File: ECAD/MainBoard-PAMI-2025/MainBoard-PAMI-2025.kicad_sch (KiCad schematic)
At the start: 53 parts, among them J1 Sensor_Center, J10 Serial, J11 Con_Batt, J13 OLED, J2 USB_B, J3 Sensor_RIGHT, J4 Servo, J5 Sensor_LEFT, J6 Servo, J7 LeftMotor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

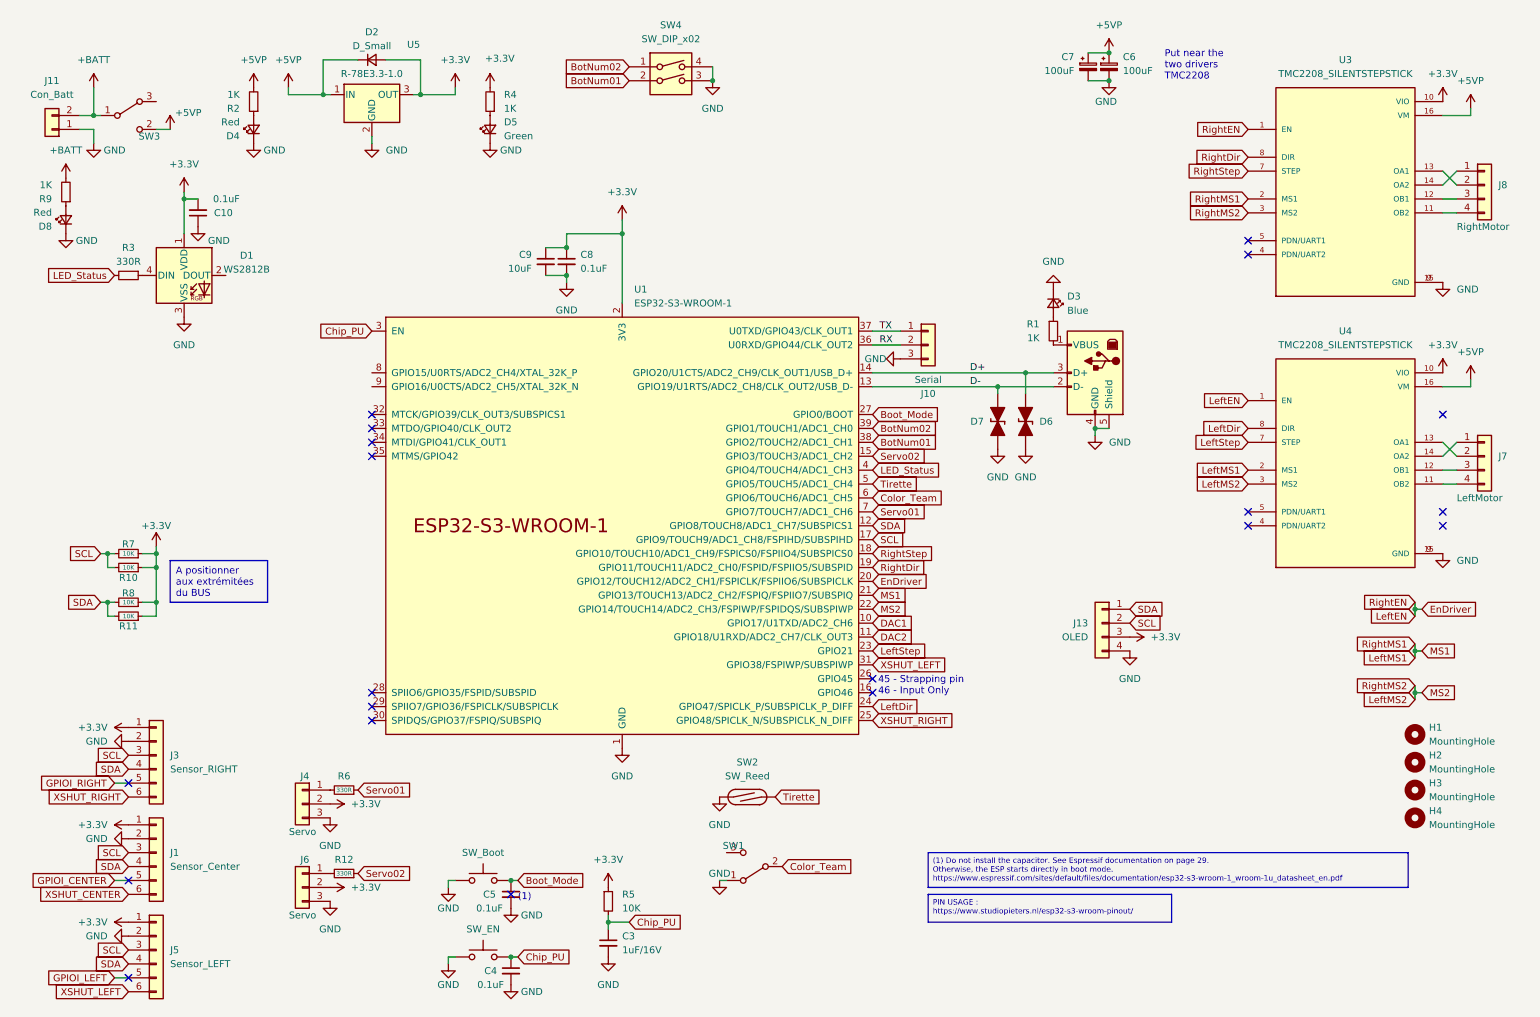
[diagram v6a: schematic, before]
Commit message: Update Live 206
Update Battery
Add Recom 5V
Add ASM1117
Add capacitor
Change sensor header
Move components
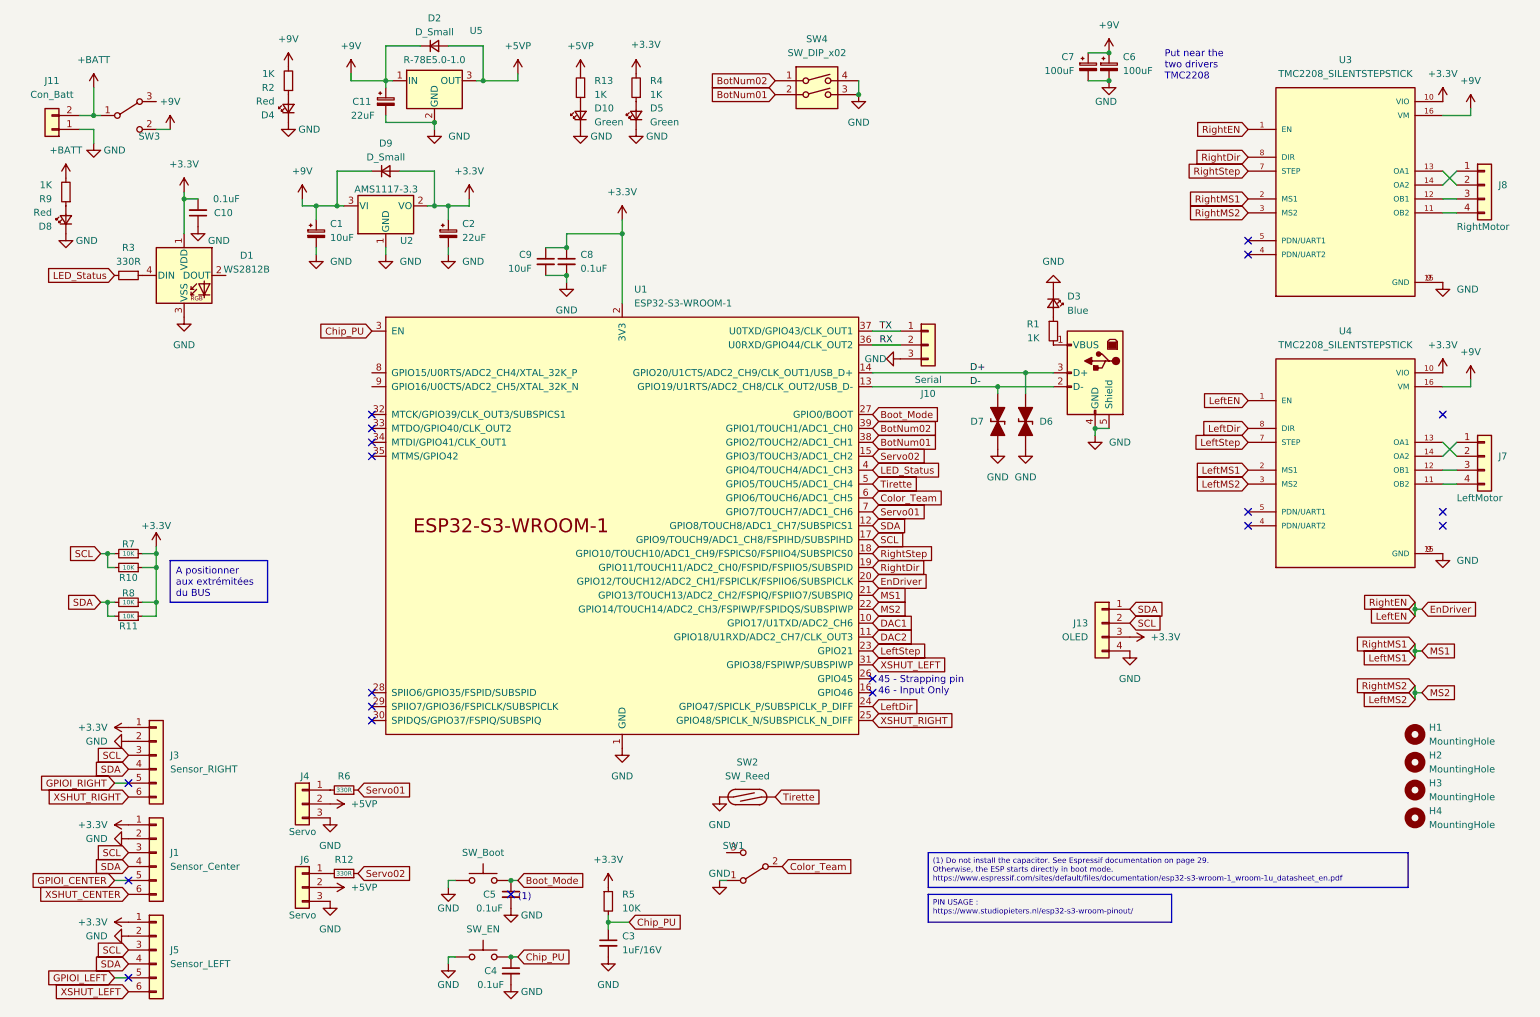
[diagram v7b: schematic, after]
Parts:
- added C1: 10uF, Capacitor_SMD:CP_Elec_5x5.4, symbol Device:C_Polarized_Small
- added C11: 22uF, Capacitor_SMD:CP_Elec_5x5.4, symbol Device:CP_Small
- added C2: 22uF, Capacitor_Tantalum_SMD:CP_EIA-3528-12_Kemet-T_Pad1.50x2.35mm_HandSolder, symbol Device:C_Polarized_Small
- added D10: Green, LED_SMD:LED_1206_3216Metric, symbol Device:LED_Small
- added D9: D_Small, Diode_SMD:D_SMA_Handsoldering, symbol Device:D_Small
- added R13: 1K, Resistor_SMD:R_1206_3216Metric_Pad1.30x1.75mm_HandSolder, symbol Device:R_Small
- added U2: AMS1117-3.3, Package_TO_SOT_SMD:SOT-223-3_TabPin2, symbol Regulator_Linear:AMS1117-3.3
- J1, J3, J5: footprint Connector_PinSocket_2.54mm:PinSocket_1x06_P2.54mm_Vertical -> PAMI-2025:VL53 Bottom Entry Version
- J11: footprint PAMI-2025:LP-e6 Batterie -> Connector_Molex:Molex_KK-254_AE-6410-02A_1x02_P2.54mm_Vertical
- U5: value R-78E3.3-1.0 -> R-78E5.0-1.0
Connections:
- net +3.3V: now also C2.1, D9.2 (A), U2.2 (VO); no longer D2.2 (A), J4.2 (Pin_2), J6.2 (Pin_2), U5.3 (OUT)
- net +5VP: now also D2.2 (A), J4.2 (Pin_2), J6.2 (Pin_2), U5.3 (OUT), R13.2; no longer C6.1, C7.1, D2.1 (K), R2.2, SW3.2 (C), U3.16 (VM), U4.16 (VM), U5.1 (IN)
- net GND: now also C1.2, C11.2, C2.2, D10.1 (K), U2.1 (GND)
- new net: D10.2 (A), R13.1
- new net +9V: C1.1, C11.1, C6.1, C7.1, D2.1 (K), D9.1 (K), R2.2, SW3.2 (C), U2.3 (VI), U3.16 (VM), U4.16 (VM), U5.1 (IN)
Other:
- moved on the sheet: D2, D4, D5, R2, R4, SW4, U5

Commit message: Add buzzer
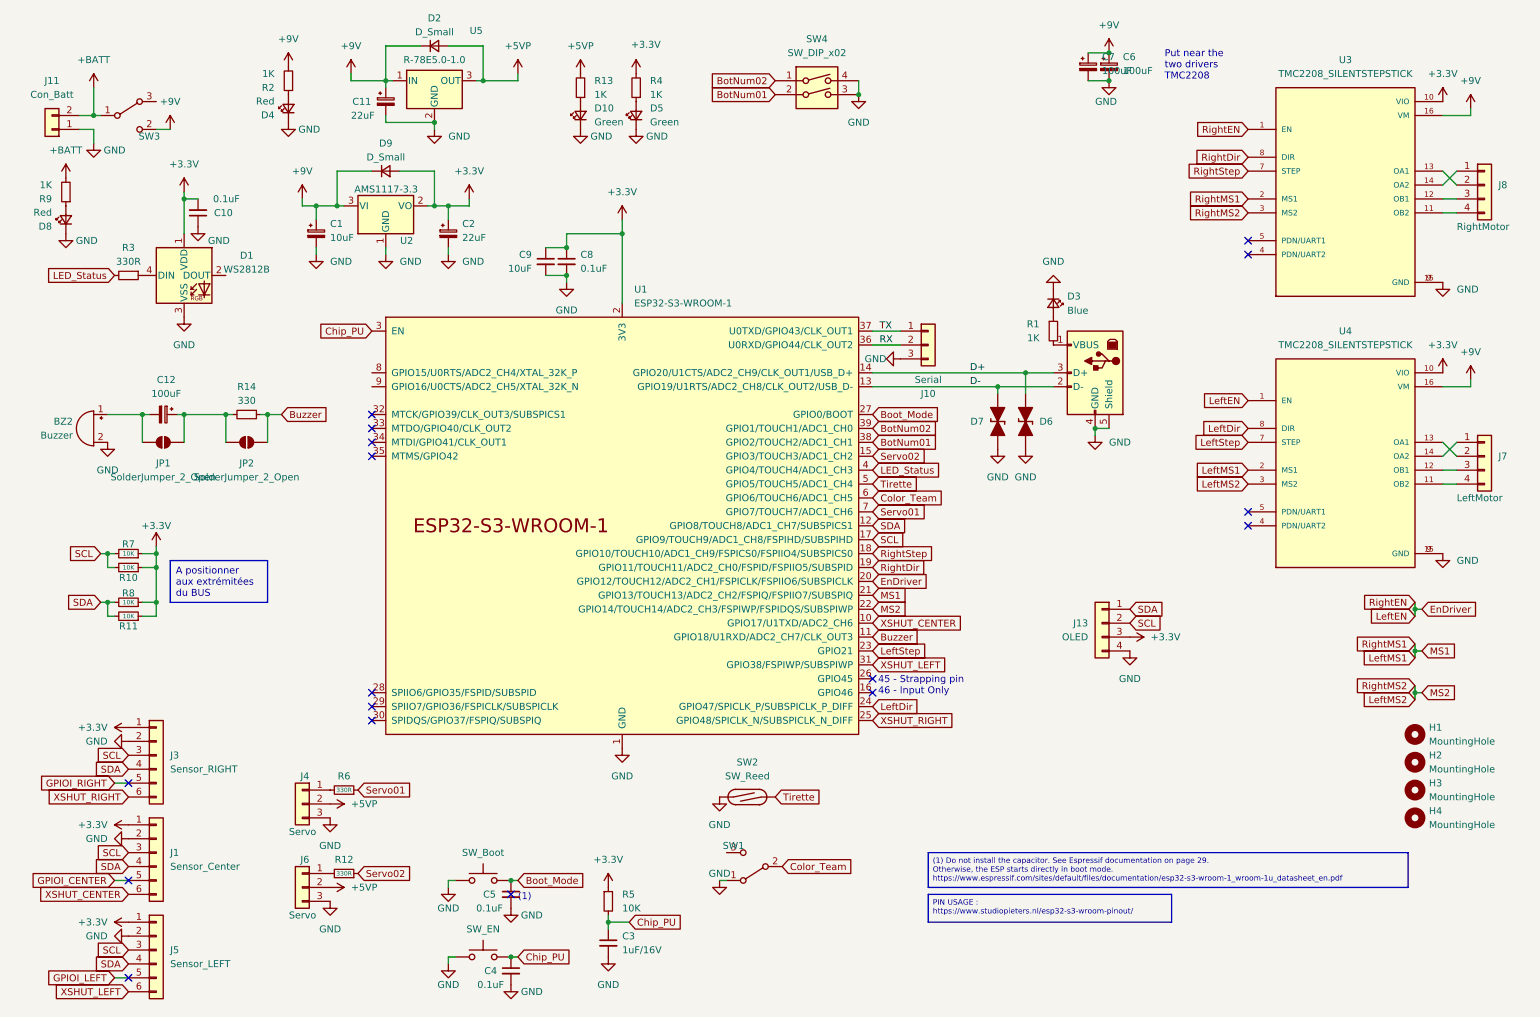
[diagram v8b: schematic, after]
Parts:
- added BZ2: Buzzer, Buzzer_Beeper:Buzzer_12x9.5RM7.6, symbol Device:Buzzer
- added C12: 100uF, Capacitor_SMD:CP_Elec_5x5.4, symbol Device:CP_Small
- added JP1, JP2: SolderJumper_2_Open, Jumper:SolderJumper-2_P1.3mm_Open_RoundedPad1.0x1.5mm, symbol Jumper:SolderJumper_2_Open
- added R14: 330, Resistor_SMD:R_1206_3216Metric_Pad1.30x1.75mm_HandSolder, symbol Device:R_Small
- C6, C7: footprint Capacitor_THT:CP_Radial_D8.0mm_P3.80mm -> Capacitor_THT:CP_Radial_D8.0mm_P3.50mm
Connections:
- net DAC1 is gone; now on net XSHUT_CENTER: U1.10 (GPIO17/U1TXD/ADC2_CH6)
- net GND: now also BZ2.2 (-)
- net DAC2 renamed Buzzer
- net Buzzer: now also JP2.2 (B), R14.1
- new net: C12.1, JP1.2 (B), JP2.1 (A), R14.2
- new net: BZ2.1 (+), C12.2, JP1.1 (A)
- no-connect marks 20 -> 17
